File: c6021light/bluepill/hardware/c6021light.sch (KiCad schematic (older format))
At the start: 71 parts, among them J1 Barrel_Jack_Switch, J10 Conn_01x02, J11 Conn_01x02, J12 XpressNet, J2 Conn_02x04_Odd_Even, J3 Conn_02x16_Row_Letter_First, J30 Loconet, J4 Conn_01x02, J5 Grove I2C, J50 USB_B_Micro, J51 Conn_01x06, J52 Debug UART, J6 Conn_01x02, J7 Conn_01x02, J8 RJ45, Q30 BC337, SW1 SW_Push, U1 L7805, U10 SN75176, U2 L7808, U3 MCP2562, U30 LM393, U4 ISO1050DUB, U50 CH340C

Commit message: more fixes
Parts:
- added J31: Conn_01x02, Connector_PinHeader_2.54mm:PinHeader_1x02_P2.54mm_Vertical, symbol Connector_Generic:Conn_01x02
- added Q31, Q32: BC547, Package_TO_SOT_THT:TO-92_Inline, symbol Transistor_BJT:BC547
- added R41: 47, w_pth_resistors:RC03, symbol Device:R
- added R42: 10k, w_pth_resistors:RC03, symbol Device:R
- C10: footprint Capacitor_THT:C_Disc_D3.0mm_W2.0mm_P2.50mm -> Capacitor_THT:C_Disc_D3.0mm_W1.6mm_P2.50mm
- C3, C4, C5, C6, C7, C8: footprint Capacitor_THT:C_Disc_D5.0mm_W2.5mm_P2.50mm -> Capacitor_THT:C_Disc_D3.0mm_W1.6mm_P2.50mm
- J51: footprint Connector_PinHeader_2.00mm:PinHeader_1x06_P2.00mm_Vertical -> Connector_PinHeader_1.27mm:PinHeader_1x06_P1.27mm_Vertical
- R13, R14, R15: footprint Resistor_THT:R_Axial_DIN0207_L6.3mm_D2.5mm_P7.62mm_Horizontal -> w_pth_resistors:RC03
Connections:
- net +12V: now also J31.2 (Pin_2)
- net LN: now reaches J30.3, J30.4, R30.1
- net LN: now also Q32.3 (E), R41.1
- new net: J31.1 (Pin_1), Q31.1 (C), R42.2
- new net: Q31.2 (B), Q32.1 (C), R42.1
- new net: Q31.3 (E), Q32.2 (B), R41.2
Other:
- note added: "15mA\nStromquelle"
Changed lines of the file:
@@
 F 0 "C5" H 5900 1250 50  0000 L CNN
 F 1 "100n" H 5850 1100 50  0000 L CNN
-F 2 "Capacitor_THT:C_Disc_D5.0mm_W2.5mm_P2.50mm" H 6113 1025 50  0001 C CNN
+F 2 "Capacitor_THT:C_Disc_D3.0mm_W1.6mm_P2.50mm" H 6113 1025 50  0001 C CNN
 F 3 "~" H 6075 1175 50  0001 C CNN
 	1    6075 1175
@@
 F 0 "C6" H 6425 1250 50  0000 L CNN
 F 1 "100n" H 6425 1100 50  0000 L CNN
-F 2 "Capacitor_THT:C_Disc_D5.0mm_W2.5mm_P2.50mm" H 6413 1025 50  0001 C CNN
+F 2 "Capacitor_THT:C_Disc_D3.0mm_W1.6mm_P2.50mm" H 6413 1025 50  0001 C CNN
 F 3 "~" H 6375 1175 50  0001 C CNN
 	1    6375 1175
@@
 F 0 "C10" H 1415 7321 50  0000 L CNN
 F 1 "100nF" H 1415 7230 50  0000 L CNN
-F 2 "Capacitor_THT:C_Disc_D3.0mm_W2.0mm_P2.50mm" H 1338 7125 50  0001 C CNN
+F 2 "Capacitor_THT:C_Disc_D3.0mm_W1.6mm_P2.50mm" H 1338 7125 50  0001 C CNN
 F 3 "~" H 1300 7275 50  0001 C CNN
 	1    1300 7275
@@
 F 0 "R14" H 2370 6921 50  0000 L CNN
 F 1 "3k3" V 2300 6800 50  0000 L CNN
-F 2 "Resistor_THT:R_Axial_DIN0207_L6.3mm_D2.5mm_P7.62mm_Horizontal" V 2230 6875 50  0001 C CNN
+F 2 "w_pth_resistors:RC03" V 2230 6875 50  0001 C CNN
 F 3 "~" H 2300 6875 50  0001 C CNN
 	1    2300 6875
@@
 F 0 "R15" H 2520 6321 50  0000 L CNN
 F 1 "3k3" V 2450 6200 50  0000 L CNN
-F 2 "Resistor_THT:R_Axial_DIN0207_L6.3mm_D2.5mm_P7.62mm_Horizontal" V 2380 6275 50  0001 C CNN
+F 2 "w_pth_resistors:RC03" V 2380 6275 50  0001 C CNN
 F 3 "~" H 2450 6275 50  0001 C CNN
 	1    2450 6275
@@
 LN_RX
 $Comp
-L Connector:RJ12 J30
-U 1 1 5F4D9B61
-P 10700 5225
-F 0 "J30" H 10725 5725 50  0000 R CNN
-F 1 "Loconet" H 10875 5550 50  0000 R CNN
-F 2 "Connector_RJ:RJ12_Amphenol_54601" V 10700 5250 50  0001 C CNN
-F 3 "~" V 10700 5250 50  0001 C CNN
-	1    10700 5225
-	-1   0    0    1
-$EndComp
-$Comp
 L Connector_Generic:Conn_01x02 J11
 U 1 1 5F5534A8
@@
 F 0 "R13" H 2170 6321 50  0000 L CNN
 F 1 "120" V 2100 6200 50  0000 L CNN
-F 2 "Resistor_THT:R_Axial_DIN0207_L6.3mm_D2.5mm_P7.62mm_Horizontal" V 2030 6275 50  0001 C CNN
+F 2 "w_pth_resistors:RC03" V 2030 6275 50  0001 C CNN
 F 3 "~" H 2100 6275 50  0001 C CNN
 	1    2100 6275
@@
 F 0 "C4" H 2300 2725 50  0000 L CNN
 F 1 "100n" H 2300 2575 50  0000 L CNN
-F 2 "Capacitor_THT:C_Disc_D5.0mm_W2.5mm_P2.50mm" H 2288 2500 50  0001 C CNN
+F 2 "Capacitor_THT:C_Disc_D3.0mm_W1.6mm_P2.50mm" H 2288 2500 50  0001 C CNN
 F 3 "~" H 2250 2650 50  0001 C CNN
 	1    2250 2650
@@
 F 0 "C3" H 1525 2725 50  0000 L CNN
 F 1 "100n" H 1525 2575 50  0000 L CNN
-F 2 "Capacitor_THT:C_Disc_D5.0mm_W2.5mm_P2.50mm" H 1538 2500 50  0001 C CNN
+F 2 "Capacitor_THT:C_Disc_D3.0mm_W1.6mm_P2.50mm" H 1538 2500 50  0001 C CNN
 F 3 "~" H 1500 2650 50  0001 C CNN
 	1    1500 2650
@@
 F 0 "C7" H 7350 3975 50  0000 L CNN
 F 1 "100n" H 7325 3850 50  0000 L CNN
-F 2 "Capacitor_THT:C_Disc_D5.0mm_W2.5mm_P2.50mm" H 7588 3775 50  0001 C CNN
+F 2 "Capacitor_THT:C_Disc_D3.0mm_W1.6mm_P2.50mm" H 7588 3775 50  0001 C CNN
 F 3 "~" H 7550 3925 50  0001 C CNN
 	1    7550 3925
@@
 F 0 "C8" H 7675 3975 50  0000 L CNN
 F 1 "100n" H 7650 3850 50  0000 L CNN
-F 2 "Capacitor_THT:C_Disc_D5.0mm_W2.5mm_P2.50mm" H 7913 3775 50  0001 C CNN
+F 2 "Capacitor_THT:C_Disc_D3.0mm_W1.6mm_P2.50mm" H 7913 3775 50  0001 C CNN
 F 3 "~" H 7875 3925 50  0001 C CNN
 	1    7875 3925
@@
 	9725 5275 9775 5275
 Wire Wire Line
-	10300 5225 10175 5225
-Wire Wire Line
 	10175 5225 10175 5275
-Wire Wire Line
-	10175 5325 10300 5325
 Wire Wire Line
 	10175 5275 10125 5275
@@
 Wire Wire Line
 	8975 5625 8975 5675
-NoConn ~ 10300 5025
-NoConn ~ 10300 5525
 Wire Wire Line
 	7775 5375 7650 5375
@@
 	9375 6225 9375 6275
 Wire Wire Line
-	10300 5425 10250 5425
-Wire Wire Line
-	10250 5425 10250 5125
-Wire Wire Line
-	10250 5125 10300 5125
-Wire Wire Line
-	10250 5425 10250 5675
-Connection ~ 10250 5425
-$Comp
-L power:GND #PWR0145
-U 1 1 5FE9BB7A
-P 10250 5675
-F 0 "#PWR0145" H 10250 5425 50  0001 C CNN
-F 1 "GND" H 10255 5502 50  0000 C CNN
-F 2 "" H 10250 5675 50  0001 C CNN
-F 3 "" H 10250 5675 50  0001 C CNN
-	1    10250 5675
-	1    0    0    -1
-$EndComp
-Wire Wire Line
 	8400 5475 8425 5475
 $Comp
@@
 F 0 "J51" H 6025 6325 50  0000 L CNN
 F 1 "Conn_01x06" H 6155 6701 50  0001 L CNN
-F 2 "Connector_PinHeader_2.00mm:PinHeader_1x06_P2.00mm_Vertical" H 6075 6800 50  0001 C CNN
+F 2 "Connector_PinHeader_1.27mm:PinHeader_1x06_P1.27mm_Vertical" H 6075 6800 50  0001 C CNN
 F 3 "~" H 6075 6800 50  0001 C CNN
 	1    6075 6800
@@
 Wire Notes Line
 	250  5600 6975 5600
-Wire Notes Line
-	6975 4350 11200 4350
 Text Notes 6450 5850 0    50   ~ 0
 optional\nDebug UART
-Text Notes 10550 4600 0    50   ~ 0
+Text Notes 9900 4625 0    50   ~ 0
 optional\nLoconet
 Wire Wire Line
@@
 Wire Wire Line
 	6500 3625 6350 3625
+Text Label 10600 4225 0    50   ~ 0
+LN
+$Comp
+L power:+12V #PWR0163
+U 1 1 5F098754
+P 10325 3225
+F 0 "#PWR0163" H 10325 3075 50  0001 C CNN
+F 1 "+12V" H 10340 3398 50  0000 C CNN
+F 2 "" H 10325 3225 50  0001 C CNN
+F 3 "" H 10325 3225 50  0001 C CNN
+	1    10325 3225
+	1    0    0    -1
+$EndComp
+Wire Wire Line
+	10450 3425 10450 3375
+Wire Wire Line
+	10800 4225 10450 4225
+Wire Wire Line
+	10800 4075 10800 4225
+Wire Wire Line
+	10450 3875 10450 3925
+Connection ~ 10450 3875
+Wire Wire Line
+	10500 3875 10450 3875
+Wire Wire Line
+	10450 3825 10450 3875
+Wire Wire Line
+	10800 3625 10800 3675
+Connection ~ 10800 3625
+Wire Wire Line
+	10800 3625 10750 3625
+Wire Wire Line
+	10800 3575 10800 3625
+$Comp
+L Device:R R42
+U 1 1 5EED5B79
+P 10800 3425
+F 0 "R42" V 10700 3350 50  0000 L CNN
+F 1 "10k" V 10800 3350 50  0000 L CNN
+F 2 "w_pth_resistors:RC03" V 10730 3425 50  0001 C CNN
+F 3 "~" H 10800 3425 50  0001 C CNN
+	1    10800 3425
+	-1   0    0    1
+$EndComp
+$Comp
+L Device:R R41
+U 1 1 5EED4E9C
+P 10450 4075
+F 0 "R41" V 10350 4000 50  0000 L CNN
+F 1 "47" V 10450 4025 50  0000 L CNN
+F 2 "w_pth_resistors:RC03" V 10380 4075 50  0001 C CNN
+F 3 "~" H 10450 4075 50  0001 C CNN
+	1    10450 4075
+	-1   0    0    1
+$EndComp
+$Comp
+L Transistor_BJT:BC547 Q32
+U 1 1 5EE82FD6
+P 10700 3875
+F 0 "Q32" H 10891 3921 50  0000 L CNN
+F 1 "BC547" H 10891 3830 50  0000 L CNN
+F 2 "Package_TO_SOT_THT:TO-92_Inline" H 10900 3800 50  0001 L CIN
+F 3 "http://www.fairchildsemi.com/ds/BC/BC547.pdf" H 10700 3875 50  0001 L CNN
+	1    10700 3875
+	1    0    0    -1
+$EndComp
+$Comp
+L Transistor_BJT:BC547 Q31
+U 1 1 5EE81C3B
+P 10550 3625
+F 0 "Q31" H 10741 3671 50  0000 L CNN
+F 1 "BC547" H 10741 3580 50  0000 L CNN
+F 2 "Package_TO_SOT_THT:TO-92_Inline" H 10750 3550 50  0001 L CIN
+F 3 "http://www.fairchildsemi.com/ds/BC/BC547.pdf" H 10550 3625 50  0001 L CNN
+	1    10550 3625
+	-1   0    0    -1
+$EndComp
+Text Label 10175 5225 0    50   ~ 0
+LN
+$Comp
+L power:GND #PWR0145
+U 1 1 5FE9BB7A
+P 10250 5675
+F 0 "#PWR0145" H 10250 5425 50  0001 C CNN
+F 1 "GND" H 10255 5502 50  0000 C CNN
+F 2 "" H 10250 5675 50  0001 C CNN
+F 3 "" H 10250 5675 50  0001 C CNN
+	1    10250 5675
+	1    0    0    -1
+$EndComp
+Connection ~ 10250 5425
+Wire Wire Line
+	10250 5425 10250 5675
+Wire Wire Line
+	10250 5125 10300 5125
+Wire Wire Line
+	10250 5425 10250 5125
+Wire Wire Line
+	10300 5425 10250 5425
+NoConn ~ 10300 5525
+NoConn ~ 10300 5025
+Wire Wire Line
+	10175 5325 10300 5325
+Wire Wire Line
+	10300 5225 10175 5225
+$Comp
+L Connector:RJ12 J30
+U 1 1 5F4D9B61
+P 10700 5225
+F 0 "J30" H 10725 5725 50  0000 R CNN
+F 1 "Loconet" H 10875 5550 50  0000 R CNN
+F 2 "Connector_RJ:RJ12_Amphenol_54601" V 10700 5250 50  0001 C CNN
+F 3 "~" V 10700 5250 50  0001 C CNN
+	1    10700 5225
+	-1   0    0    1
+$EndComp
+$Comp
+L Connector_Generic:Conn_01x02 J31
+U 1 1 5F0FF03F
+P 10125 3375
+F 0 "J31" H 10300 3475 50  0000 C CNN
+F 1 "Conn_01x02" H 10043 3141 50  0001 C CNN
+F 2 "Connector_PinHeader_2.54mm:PinHeader_1x02_P2.54mm_Vertical" H 10125 3375 50  0001 C CNN
+F 3 "~" H 10125 3375 50  0001 C CNN
+	1    10125 3375
+	-1   0    0    1
+$EndComp
+Wire Wire Line
+	10450 3375 10325 3375
+Connection ~ 10450 3375
+Wire Wire Line
+	10450 3375 10450 3275
+Wire Wire Line
+	10450 3275 10800 3275
+Wire Wire Line
+	10325 3225 10325 3275
+Wire Notes Line
+	6975 4375 9825 4375
+Wire Notes Line
+	9825 4375 9825 2900
+Wire Notes Line
+	9825 2900 11225 2900
+Text Notes 9875 4025 0    50   ~ 0
+15mA\nStromquelle
 $EndSCHEMATC

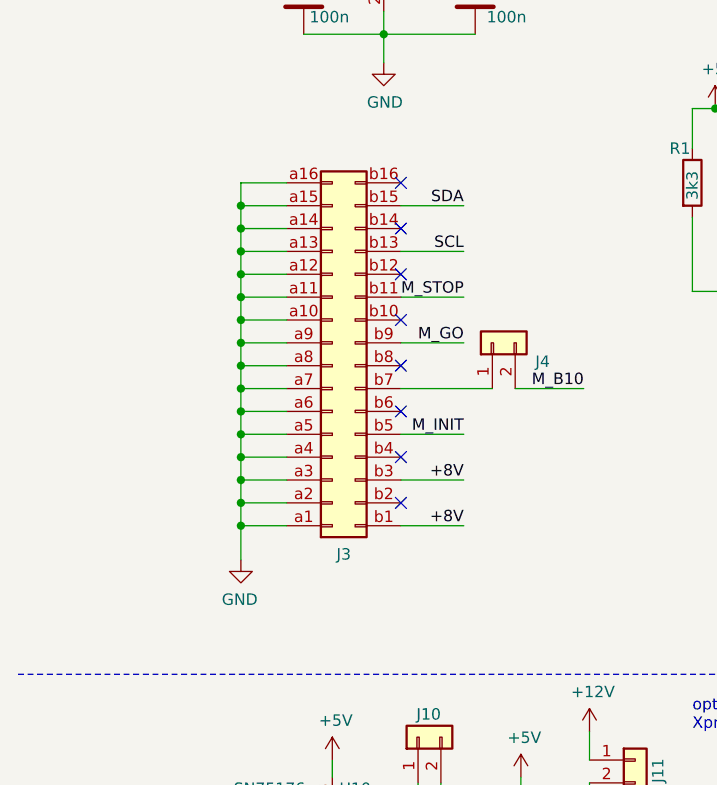
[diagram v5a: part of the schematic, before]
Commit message: fix DIN socket
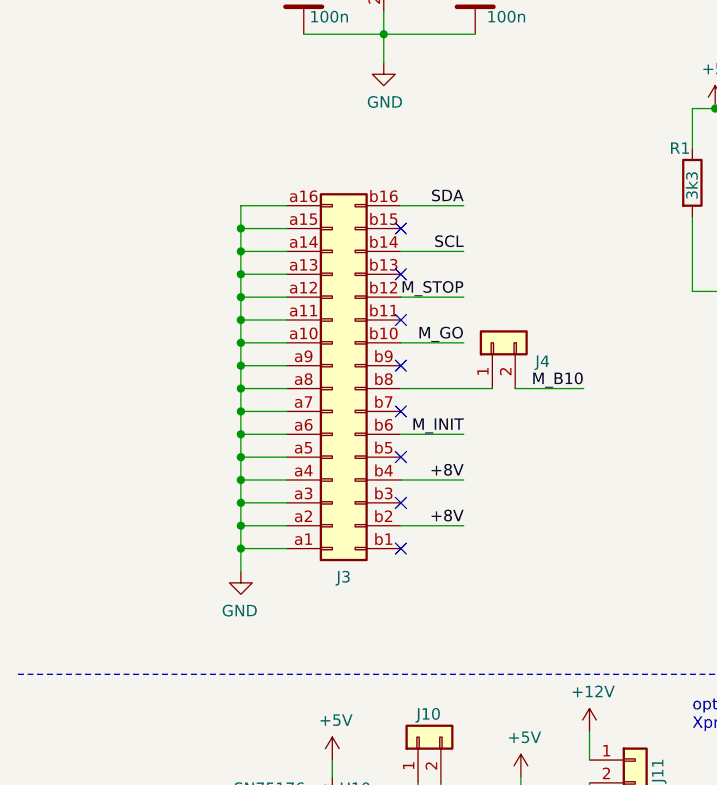
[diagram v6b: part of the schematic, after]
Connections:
- net +8V: now also J3.b2 (Pin_b2), J3.b4 (Pin_b4); no longer J3.b1 (Pin_b1), J3.b3 (Pin_b3)
- net M_GO: now also J3.b10 (Pin_b10); no longer J3.b9 (Pin_b9)
- net M_INIT: now also J3.b6 (Pin_b6); no longer J3.b5 (Pin_b5)
- net M_STOP: now also J3.b12 (Pin_b12); no longer J3.b11 (Pin_b11)
- net SCL: now also J3.b14 (Pin_b14); no longer J3.b13 (Pin_b13)
- net SDA: now also J3.b16 (Pin_b16); no longer J3.b15 (Pin_b15)
- net at J3.b7 (Pin_b7): no longer J4.1 (Pin_1)
- net at J3.b8 (Pin_b8): now also J4.1 (Pin_1)
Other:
- moved on the sheet: J3
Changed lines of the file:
@@
 NoConn ~ 1925 3850
 NoConn ~ 1925 3650
-NoConn ~ 1925 3450
+NoConn ~ 1925 5050
 Wire Wire Line
 	1925 3750 2200 3750
@@
 Wire Wire Line
 	1225 3550 1225 3650
-Connection ~ 1225 3550
 Wire Wire Line
 	1225 3650 1225 3750
@@
 Connection ~ 1225 4850
 Wire Wire Line
-	1225 4950 1225 5100
+	1225 4950 1225 5050
 Connection ~ 1225 4950
 $Comp
 L power:GND #PWR0117
 U 1 1 5EE50DE0
-P 1225 5100
-F 0 "#PWR0117" H 1225 4850 50  0001 C CNN
-F 1 "GND" H 1230 4927 50  0000 C CNN
-F 2 "" H 1225 5100 50  0001 C CNN
-F 3 "" H 1225 5100 50  0001 C CNN
-	1    1225 5100
+P 1225 5150
+F 0 "#PWR0117" H 1225 4900 50  0001 C CNN
+F 1 "GND" H 1230 4977 50  0000 C CNN
+F 2 "" H 1225 5150 50  0001 C CNN
+F 3 "" H 1225 5150 50  0001 C CNN
+	1    1225 5150
 	-1   0    0    -1
 $EndComp
-Wire Wire Line
-	1225 3450 1225 3550
 $Comp
 L Device:C C4
@@
 Wire Wire Line
 	1425 4350 1225 4350
-Wire Wire Line
-	1425 3450 1225 3450
 $Comp
 L Connector_Generic:Conn_02x16_Row_Letter_First J3
 U 1 1 5EE1C5CE
-P 1625 4250
-F 0 "J3" H 1675 5075 50  0000 C CNN
-F 1 "Conn_02x16_Row_Letter_First" H 1675 5076 50  0001 C CNN
-F 2 "Connector_DIN:DIN41612_B2_2x16_Female_Vertical_THT" H 1625 4250 50  0001 C CNN
-F 3 "~" H 1625 4250 50  0001 C CNN
-	1    1625 4250
+P 1625 4350
+F 0 "J3" H 1675 5175 50  0000 C CNN
+F 1 "Conn_02x16_Row_Letter_First" H 1675 5176 50  0001 C CNN
+F 2 "Connector_DIN:DIN41612_B2_2x16_Female_Vertical_THT" H 1625 4350 50  0001 C CNN
+F 3 "~" H 1625 4350 50  0001 C CNN
+	1    1625 4350
 	1    0    0    1
 $EndComp
@@
 Text Notes 9875 4025 0    50   ~ 0
 15mA\nStromquelle
+Wire Wire Line
+	1425 5050 1225 5050
+Connection ~ 1225 5050
+Wire Wire Line
+	1225 5050 1225 5150
 $EndSCHEMATC

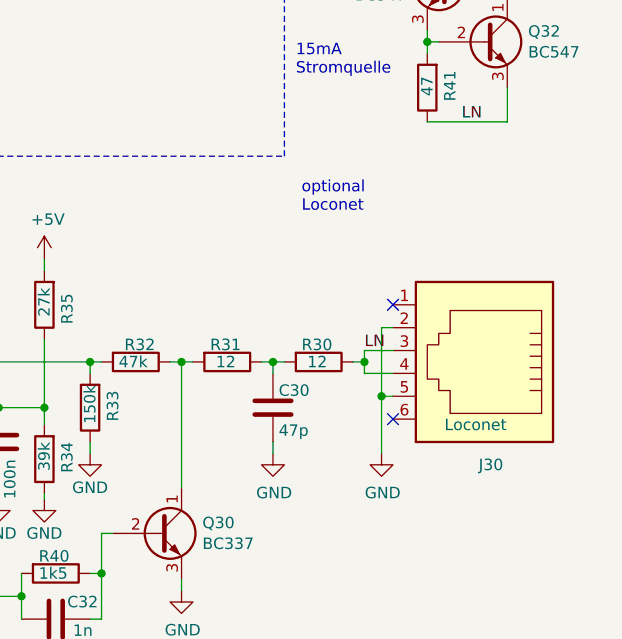
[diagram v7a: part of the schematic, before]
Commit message: add 12V power supply option for Loconet / chnage 1x2 pinh header footprint
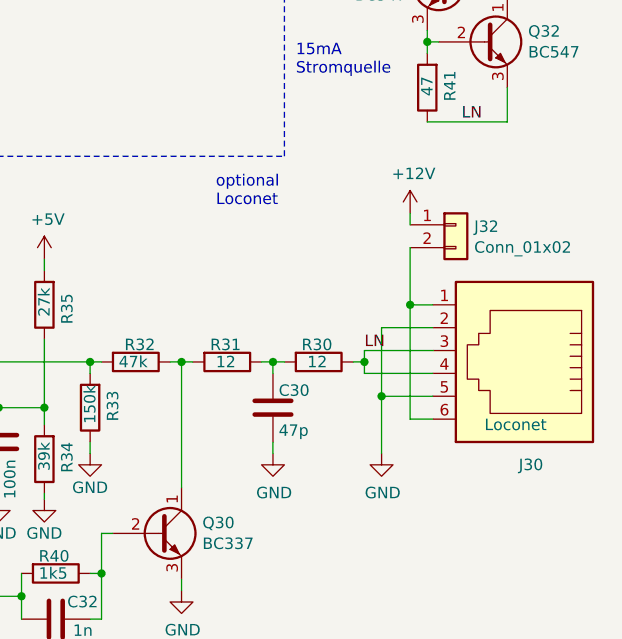
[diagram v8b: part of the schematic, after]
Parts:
- added J32: Conn_01x02, Connector_PinHeader_2.54mm:PinHeader_1x02_P2.54mm_Vertical_NB, symbol Connector_Generic:Conn_01x02
- J10, J11, J31, J4, J6, J7: footprint Connector_PinHeader_2.54mm:PinHeader_1x02_P2.54mm_Vertical -> Connector_PinHeader_2.54mm:PinHeader_1x02_P2.54mm_Vertical_NB
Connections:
- net +12V: now also J32.1 (Pin_1)
- net at J30.1: now also J30.6, J32.2 (Pin_2)
- no-connect marks 26 -> 24
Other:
- moved on the sheet: J30
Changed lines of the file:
@@
 F 0 "J7" V 8643 1080 50  0000 L CNN
 F 1 "Conn_01x02" V 8688 1080 50  0001 L CNN
-F 2 "Connector_PinHeader_2.54mm:PinHeader_1x02_P2.54mm_Vertical" H 8725 1000 50  0001 C CNN
+F 2 "Connector_PinHeader_2.54mm:PinHeader_1x02_P2.54mm_Vertical_NB" H 8725 1000 50  0001 C CNN
 F 3 "~" H 8725 1000 50  0001 C CNN
 	1    8725 1000
@@
 F 0 "J10" V 2100 5775 50  0000 L CNN
 F 1 "Conn_01x02" V 1963 5955 50  0001 L CNN
-F 2 "Connector_PinHeader_2.54mm:PinHeader_1x02_P2.54mm_Vertical" H 2000 5875 50  0001 C CNN
+F 2 "Connector_PinHeader_2.54mm:PinHeader_1x02_P2.54mm_Vertical_NB" H 2000 5875 50  0001 C CNN
 F 3 "~" H 2000 5875 50  0001 C CNN
 	1    2000 5875
@@
 F 0 "J6" V 8243 755 50  0000 L CNN
 F 1 "Conn_01x02" V 8288 755 50  0001 L CNN
-F 2 "Connector_PinHeader_2.54mm:PinHeader_1x02_P2.54mm_Vertical" H 8325 675 50  0001 C CNN
+F 2 "Connector_PinHeader_2.54mm:PinHeader_1x02_P2.54mm_Vertical_NB" H 8325 675 50  0001 C CNN
 F 3 "~" H 8325 675 50  0001 C CNN
 	1    8325 675
@@
 F 0 "J11" V 3050 5875 50  0000 L CNN
 F 1 "Conn_01x02" V 2913 6055 50  0001 L CNN
-F 2 "Connector_PinHeader_2.54mm:PinHeader_1x02_P2.54mm_Vertical" H 2950 5975 50  0001 C CNN
+F 2 "Connector_PinHeader_2.54mm:PinHeader_1x02_P2.54mm_Vertical_NB" H 2950 5975 50  0001 C CNN
 F 3 "~" H 2950 5975 50  0001 C CNN
 	1    2950 5975
@@
 Text Notes 6450 5850 0    50   ~ 0
 optional\nDebug UART
-Text Notes 9900 4625 0    50   ~ 0
+Text Notes 9525 4600 0    50   ~ 0
 optional\nLoconet
 Wire Wire Line
@@
 F 0 "J4" V 2243 3962 50  0000 R CNN
 F 1 "Conn_01x02" V 2198 3962 50  0001 R CNN
-F 2 "Connector_PinHeader_2.54mm:PinHeader_1x02_P2.54mm_Vertical" H 2325 4150 50  0001 C CNN
+F 2 "Connector_PinHeader_2.54mm:PinHeader_1x02_P2.54mm_Vertical_NB" H 2325 4150 50  0001 C CNN
 F 3 "~" H 2325 4150 50  0001 C CNN
 	1    2325 4150
@@
 	10250 5425 10250 5675
 Wire Wire Line
-	10250 5125 10300 5125
+	10250 5125 10475 5125
 Wire Wire Line
 	10250 5425 10250 5125
 Wire Wire Line
-	10300 5425 10250 5425
-NoConn ~ 10300 5525
-NoConn ~ 10300 5025
-Wire Wire Line
-	10175 5325 10300 5325
-Wire Wire Line
-	10300 5225 10175 5225
-$Comp
-L Connector:RJ12 J30
-U 1 1 5F4D9B61
-P 10700 5225
-F 0 "J30" H 10725 5725 50  0000 R CNN
-F 1 "Loconet" H 10875 5550 50  0000 R CNN
-F 2 "Connector_RJ:RJ12_Amphenol_54601" V 10700 5250 50  0001 C CNN
-F 3 "~" V 10700 5250 50  0001 C CNN
-	1    10700 5225
-	-1   0    0    1
-$EndComp
+	10475 5425 10250 5425
+Wire Wire Line
+	10175 5325 10475 5325
+Wire Wire Line
+	10475 5225 10175 5225
 $Comp
 L Connector_Generic:Conn_01x02 J31
@@
 F 0 "J31" H 10300 3475 50  0000 C CNN
 F 1 "Conn_01x02" H 10043 3141 50  0001 C CNN
-F 2 "Connector_PinHeader_2.54mm:PinHeader_1x02_P2.54mm_Vertical" H 10125 3375 50  0001 C CNN
+F 2 "Connector_PinHeader_2.54mm:PinHeader_1x02_P2.54mm_Vertical_NB" H 10125 3375 50  0001 C CNN
 F 3 "~" H 10125 3375 50  0001 C CNN
 	1    10125 3375
@@
 Wire Wire Line
 	1225 5050 1225 5150
+$Comp
+L Connector:RJ12 J30
+U 1 1 5F4D9B61
+P 10875 5225
+F 0 "J30" H 10900 5725 50  0000 R CNN
+F 1 "Loconet" H 11050 5550 50  0000 R CNN
+F 2 "Connector_RJ:RJ12_Amphenol_54601" V 10875 5250 50  0001 C CNN
+F 3 "~" V 10875 5250 50  0001 C CNN
+	1    10875 5225
+	-1   0    0    1
+$EndComp
+Wire Wire Line
+	10475 5025 10375 5025
+Wire Wire Line
+	10375 5025 10375 5525
+Wire Wire Line
+	10375 5525 10475 5525
+$Comp
+L Connector_Generic:Conn_01x02 J32
+U 1 1 5EE98DB5
+P 10575 4675
+F 0 "J32" H 10655 4667 50  0000 L CNN
+F 1 "Conn_01x02" H 10655 4576 50  0000 L CNN
+F 2 "Connector_PinHeader_2.54mm:PinHeader_1x02_P2.54mm_Vertical_NB" H 10575 4675 50  0001 C CNN
+F 3 "~" H 10575 4675 50  0001 C CNN
+	1    10575 4675
+	1    0    0    -1
+$EndComp
+$Comp
+L power:+12V #PWR0164
+U 1 1 5EE99FAA
+P 10375 4625
+F 0 "#PWR0164" H 10375 4475 50  0001 C CNN
+F 1 "+12V" H 10390 4798 50  0000 C CNN
+F 2 "" H 10375 4625 50  0001 C CNN
+F 3 "" H 10375 4625 50  0001 C CNN
+	1    10375 4625
+	1    0    0    -1
+$EndComp
+Wire Wire Line
+	10375 4625 10375 4675
+Wire Wire Line
+	10375 4775 10375 5025
+Connection ~ 10375 5025
 $EndSCHEMATC
